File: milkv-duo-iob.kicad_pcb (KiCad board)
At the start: 2 copper layers, 73.5 x 57.7 mm, 18 parts, among them J1 Conn_01x20_Socket, J10 Conn_01x02, J2 Conn_01x20_Socket, J3 Conn_01x05_Socket, J4 8P8C_Shielded, J5 Conn_01x20, J6 Conn_01x20, J7 Conn_01x12, J8 Conn_01x12, J9 Conn_01x04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

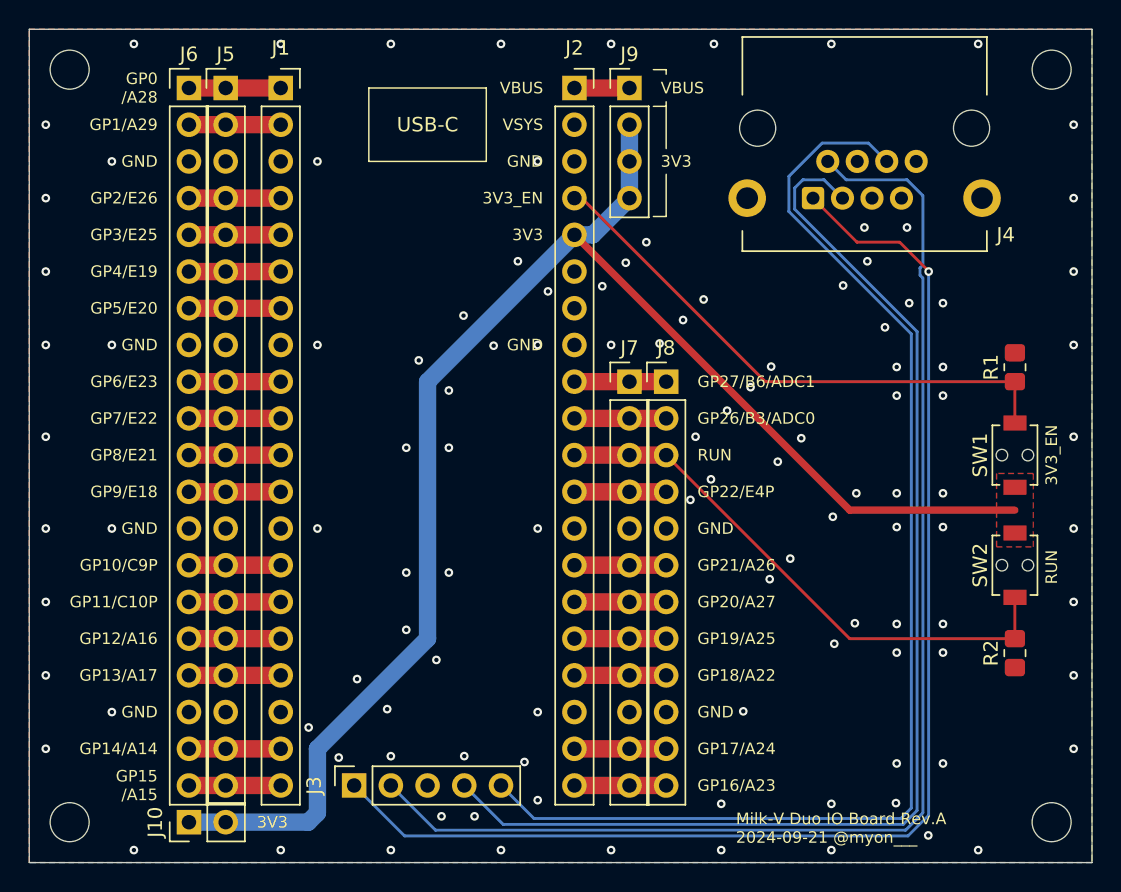
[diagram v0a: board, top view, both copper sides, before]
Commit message: Rev.A (今度こそ)
Milk-V Duo の横幅間違えてるし、公式配布の CAD 見ると Ethernet のピンが若干ずれているのも判明
Symbox/footprint 作って対応
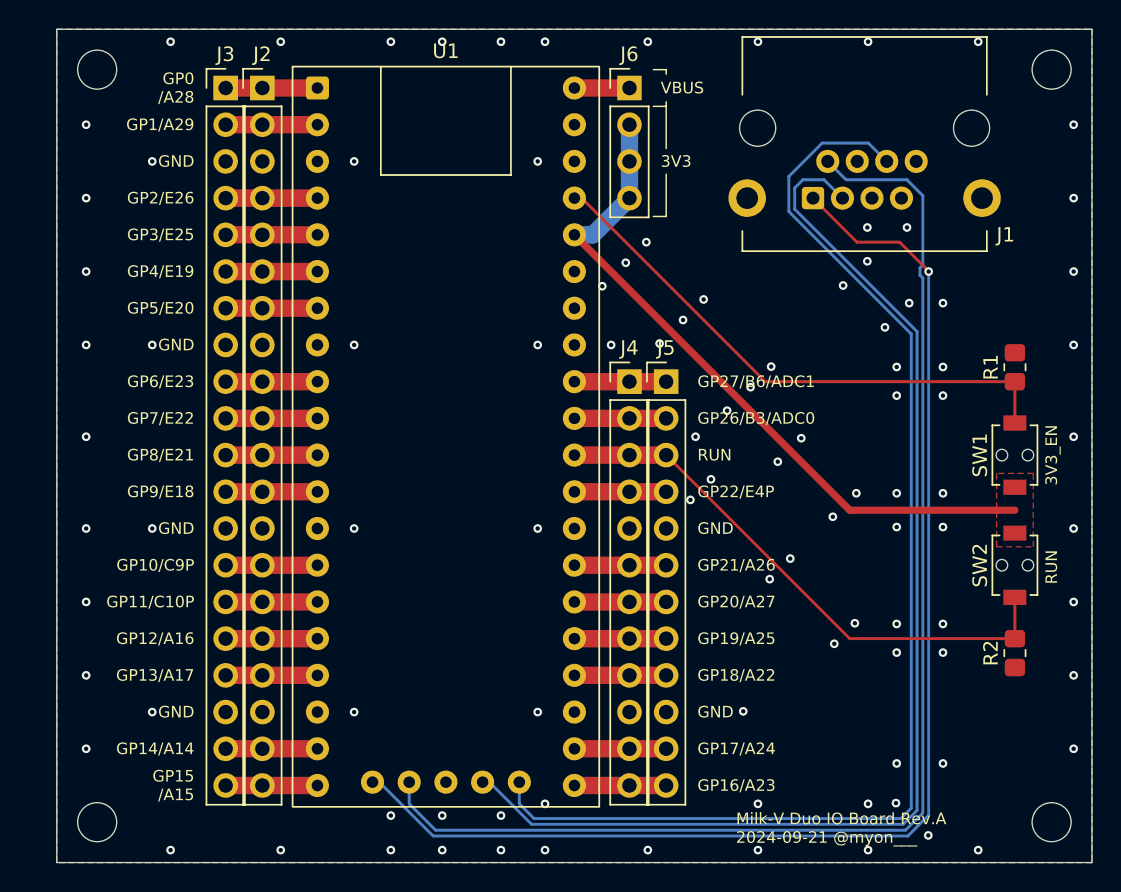
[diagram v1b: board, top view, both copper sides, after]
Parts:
- removed the J1 at (99.1, 50.8)
- removed J10: Conn_01x02, Connector_PinHeader_2.54mm:PinHeader_1x02_P2.54mm_Vertical
- removed the J2 at (119.4, 50.8)
- removed the J3 at (104.1, 99.1)
- added U1: Milk-V Duo, Library:Milk-V_Duo_THT, F.Cu at (101.6, 50.8)
- moved J2 2.54 mm to (97.8, 50.8)
- moved J3 2.54 mm to (95.2, 50.8)
- moved H3 1.91 mm to (86.4, 101.6)
- moved H4 1.91 mm to (86.4, 49.5)
- renumbered J4 to J1, J5 to J2, J6 to J3, J7 to J4, J8 to J5, J9 to J6
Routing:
- net 3V3: track 104.8 -> 48.3 mm
- net /ETH-RX+: track 83.5 -> 82.3 mm
- net /ETH-TX+: track 89.5 -> 88.4 mm
- net GND: vias 114 -> 101
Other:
- board size 73.5 x 57.7 mm -> 71.6 x 57.7 mm
- board text removed: "USB-C"
- board text removed: "VSYS"
